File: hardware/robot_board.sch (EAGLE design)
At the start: 113 parts, among them J1 POWER_JACKPTH, U2 FT232RLSSOP

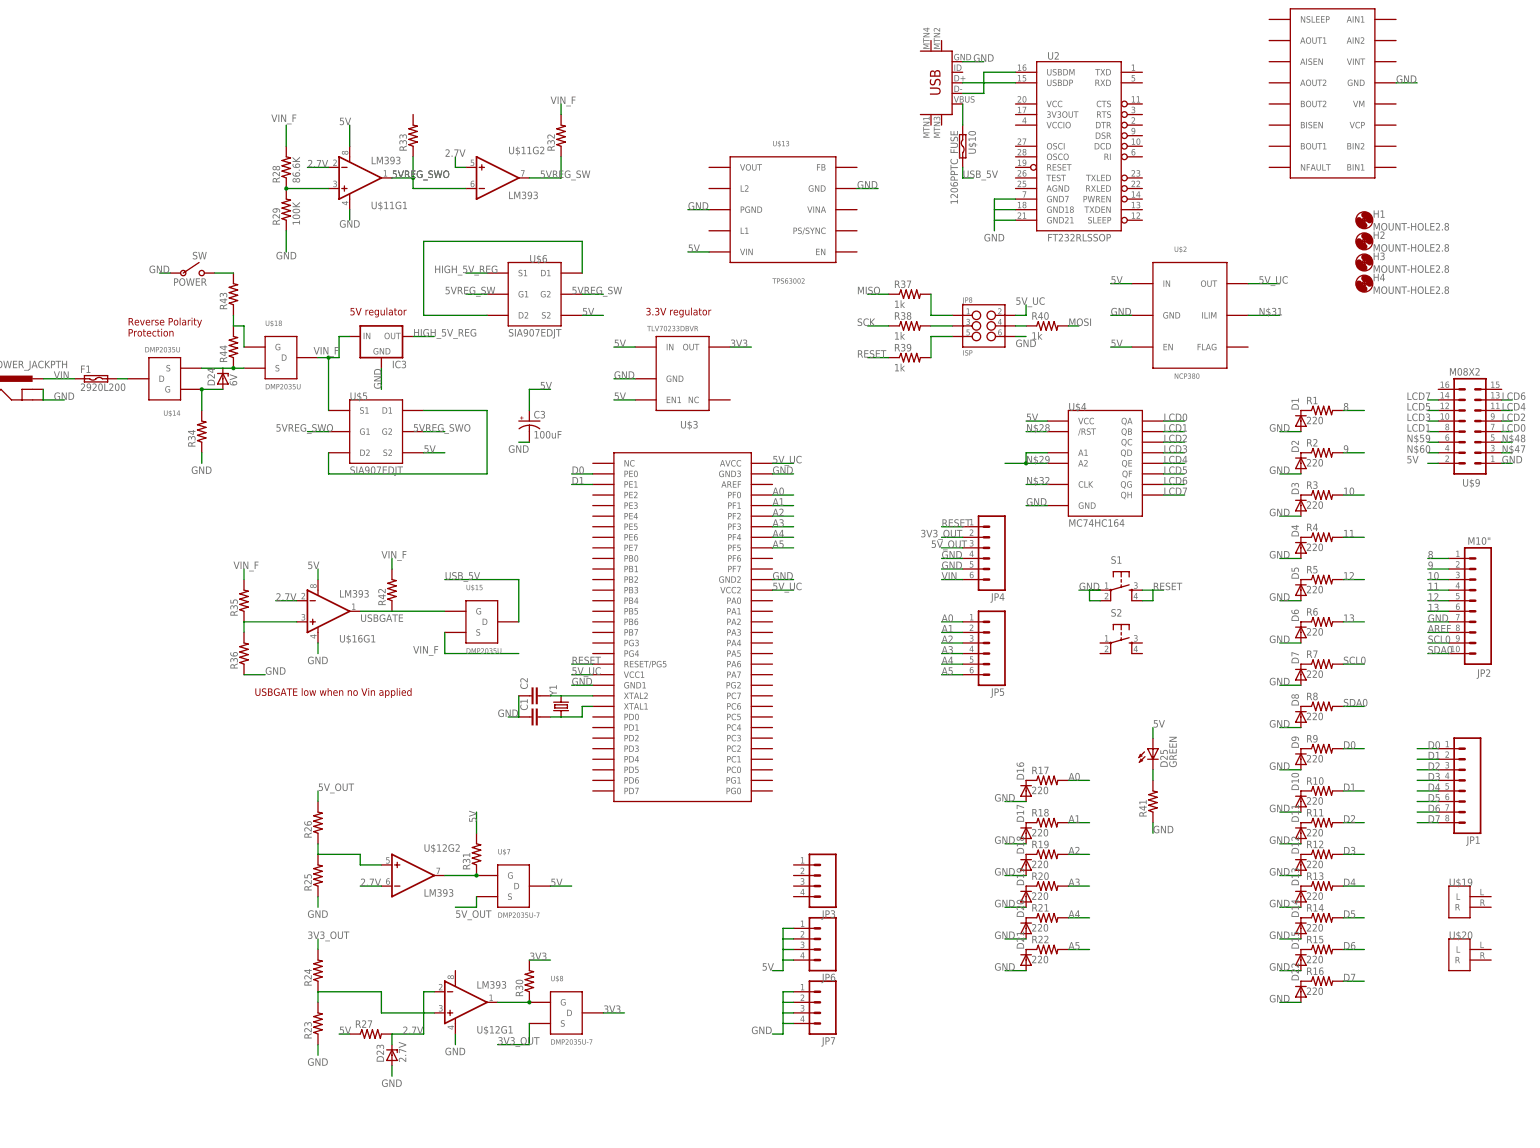
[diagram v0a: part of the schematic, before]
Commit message: check in library and restructured directories
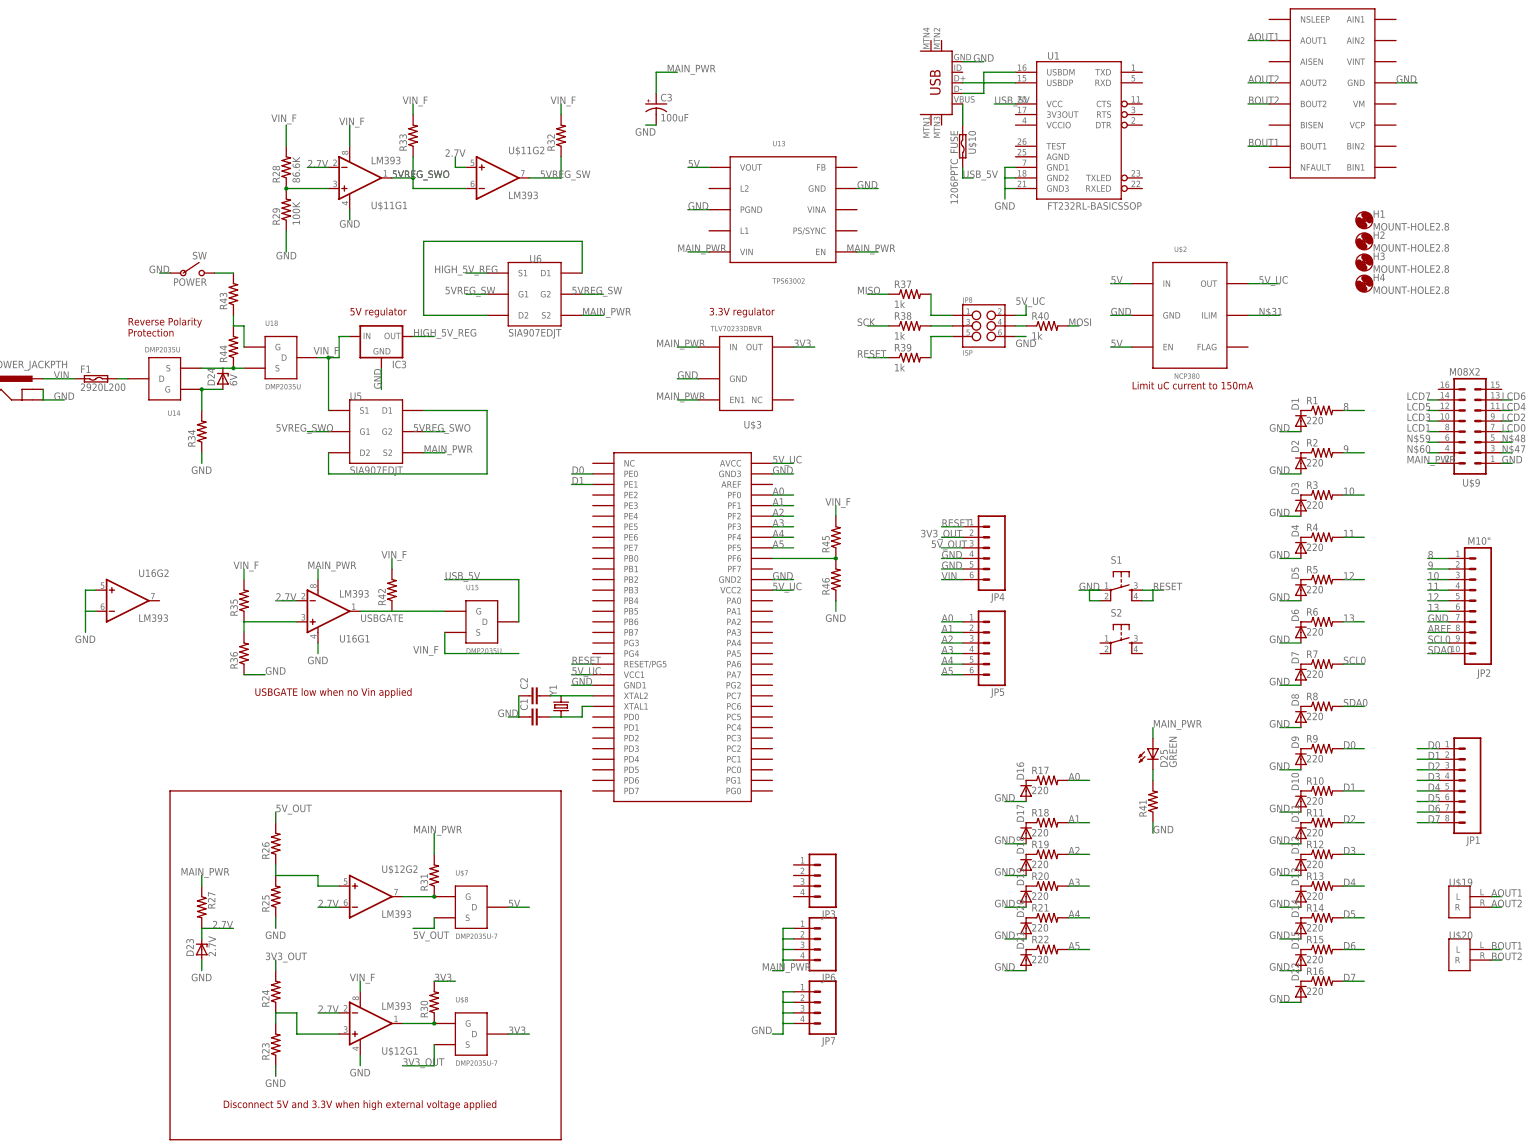
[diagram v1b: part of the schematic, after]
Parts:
- removed U$4: MC74HC164, r_cubed:MC74HC164
- removed U2: FT232RLSSOP, SparkFun-DigitalIC:FT232RLSSOP
- added R45, R46: (no value), resistor:R-US_R1206
- added U1: FT232RL-BASICSSOP, SparkFun-DigitalIC:FT232RL-BASICSSOP
- renumbered U$13 to U13, U$14 to U14, U$15 to U15, U$16 to U16, U$17 to U17, U$18 to U18, U$5 to U5, U$6 to U6
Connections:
- removed net N$28: U$4./RST
- removed net N$29: U$4.A1, U$4.A2
- removed net N$32: U$4.CLK
- new net AOUT1: U$19.L, U$21.AOUT1
- new net AOUT2: U$19.R, U$21.AOUT2
- new net BOUT1: U$20.L, U$21.BOUT1
- new net BOUT2: U$20.R, U$21.BOUT2
- new net MAIN_PWR: C3.+, D25.A, JP6.1, JP6.2, JP6.3, JP6.4, R27.1, R31.2, U$3.EN1, U$3.IN, U$9.2, U13.EN, U13.VIN, U16G1.V+, U5.S2, U6.S2
- new net N$52: R45.1, R46.2, U17.PF6
- net 5V: now also U13.VOUT; no longer C3.+, D25.A, JP6.1, JP6.2, JP6.3, JP6.4, R27.1, R31.2, U$11G1.V+, U$3.EN1, U$3.IN, U$4.VCC, U$9.2, U13.VIN, U16G1.V+, U5.S2, U6.S2
- net GND: now also R46.1, U16G2.+IN, U16G2.-IN; no longer U$4.GND, U2.GND18, U2.GND21, U2.GND7
- net LCD0: no longer U$4.QA
- net LCD1: no longer U$4.QB
- net LCD2: no longer U$4.QC
- net LCD3: no longer U$4.QD
- net LCD4: no longer U$4.QE
- net LCD5: no longer U$4.QF
- net LCD6: no longer U$4.QG
- net LCD7: no longer U$4.QH
- net N$1: now also U1.USBDM; no longer U2.USBDM
- net N$2: now also U1.USBDP; no longer U2.USBDP
- net USB_5V: now also U1.VCC
- net VIN_F: now also R33.2, R45.2, U$11G1.V+, U$12G1.V+
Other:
- note added: "Disconnect 5V and 3.3V when high external voltage applied"
- note added: "Limit uC current to 150mA"
- moved on the sheet: C3, D23, R23, R24, R25, R26, R27, R30, R31, U$12G1, U$12G2, U$3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

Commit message: updated schematic
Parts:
- removed U15: DMP2035U, jseng:DMP2035U
- added D26, D27, D28, D29: (no value), SparkFun-DiscreteSemi:DIODESOT23
- added R47, R48, R49, R50: 220, resistor:R-US_R1206
- added U2: NCP380, jseng:NCP380
- R30, R31, R32, R33, R34, R42: value (none) -> 10K
- U$2: value NCP380 -> SIA907EDJT; device jseng:NCP380 -> jseng:SIA907EDJT
- renumbered U$10 to F2, U$12 to U12, U$3 to U3, U$7 to U7, U$8 to U8
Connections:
- new net N$28: U$2.D1, U$2.D2
- new net N$29: D26.C, R47.1
- new net N$32: D27.C, R48.1
- new net N$53: D28.C, R49.1
- new net N$54: D29.C, R50.1
- new net SERVO0: JP3.1, R47.2
- new net SERVO1: JP3.2, R48.2
- new net SERVO2: JP3.3, R49.2
- new net SERVO3: JP3.4, R50.2
- net 5V: now also U13.FB, U2.EN, U2.IN; no longer U$2.EN, U$2.IN
- net 5V_UC: now also U2.OUT; no longer U$2.OUT
- net GND: now also D26.A, D27.A, D28.A, D29.A, U1.AGND, U1.GND1, U1.GND2, U1.GND3, U2.GND; no longer U$2.GND
- net MAIN_PWR: now also U13.PS/SYNC, U13.VINA
- net N$31: now also U2.ILIM; no longer U$2.ILIM
- net USBGATE: now also U$2.G1, U$2.G2; no longer U15.G
- net USB_5V: now also U$2.S1; no longer U15.D
- net VIN_F: now also U$2.S2; no longer U15.S
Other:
- note added: "Step-down 5V regulator"
- note added: "Step-up 5V regulator"
- note removed: "5V regulator"
- moved on the sheet: U$2

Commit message: update libraries
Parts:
- removed U$21: DRV8833, jseng:DRV8833
- added U$3: NRSINDUCTOR, jseng:NRSINDUCTOR
- added U$4, U$5: DRV8839, jseng:DRV8839
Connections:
- new net N$55: U$3.2, U13.L2
- new net N$56: U$3.1, U13.L1
- new net N$58: U$4.VM1, U$4.VM2
- new net N$61: U$5.VM1, U$5.VM2
- net 5V: now also U$4.NSLEEP, U$4.VCC, U$5.NSLEEP, U$5.VCC
- net AOUT1: now also U$4.OUT1; no longer U$21.AOUT1
- net AOUT2: now also U$4.OUT2; no longer U$21.AOUT2
- net BOUT1: now also U$5.OUT1; no longer U$21.BOUT1
- net BOUT2: now also U$5.OUT2; no longer U$21.BOUT2
- net GND: now also U$4.GND1, U$4.GND2, U$5.GND1, U$5.GND2; no longer U$21.GND
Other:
- moved on the sheet: D16, D17, D18, D19, D20, D21, D25, JP4, JP5, R17, R18, R19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

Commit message: added accelerometer device
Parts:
- removed U2: NCP380, jseng:NCP380
- removed U3: TLV70233DBVR, jseng:TLV70233DBVR
- added D30: GREEN, SparkFun-LED:LED-GREENLILYPAD
- added D31: YELLOW, SparkFun-LED:LED-GREENLILYPAD
- added R51, R52: 330, resistor:R-US_R1206
- added R53: 1.5K, resistor:R-US_R1206
- added R54: 10K, resistor:R-US_R1206
- added R55: 1K, resistor:R-US_R1206
- added U$6: MIC2009A, jseng:MIC2009A
- added U$7: TLV70233, jseng:TLV70233
- D23: value 2.7V -> 2.1V
- D25: value GREEN -> POWER
- R41: value (none) -> 330
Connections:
- net 10 renamed D10
- net 11 renamed D11
- net 12 renamed D12
- net 13 renamed D13
- net 2.7V renamed 2.1V
- net 8 renamed D8
- net 9 renamed D9
- net N$20 renamed D7_IN
- net N$29 renamed SERVO0_IN
- net N$32 renamed SERVO1_IN
- net N$5 renamed D8_IN
- net N$53 renamed SERVO2_IN
- net N$54 renamed SERVO3_IN
- net N$6 renamed D9_IN
- removed net N$10: D6.C, R6.1
- removed net N$11: D7.C, R7.1
- removed net N$12: D8.C, R8.1
- removed net N$13: D9.C, R9.1
- removed net N$14: D10.C, R10.1
- removed net N$15: D11.C, R11.1
- removed net N$16: D12.C, R12.1
- removed net N$17: D13.C, R13.1
- removed net N$18: D14.C, R14.1
- removed net N$19: D15.C, R15.1
- removed net N$21: D16.C, R17.1
- removed net N$22: D17.C, R18.1
- removed net N$23: D18.C, R19.1
- removed net N$24: D19.C, R20.1
- removed net N$25: D20.C, R21.1
- removed net N$26: D21.C, R22.1
- removed net N$31: U2.ILIM
- removed net N$58: U$4.VM1, U$4.VM2
- removed net N$61: U$5.VM1, U$5.VM2
- removed net N$7: D3.C, R3.1
- removed net N$8: D4.C, R4.1
- removed net N$9: D5.C, R5.1
- new net A0_IN: D16.C, R17.1, U17.PF0(ADC0)
- new net A1_IN: D17.C, R18.1, U17.PF1(ADC1)
- new net A2_IN: D18.C, R19.1, U17.PF2(ADC2)
- new net A3_IN: D19.C, R20.1, U17.PF3(ADC3)
- new net A4_IN: D20.C, R21.1, U17.PF4(ADC4)
- new net A5_IN: D21.C, R22.1, U17.PF5(ADC5)
- new net D0_IN: D9.C, R9.1, U17.PE0(TXD)
- new net D1_IN: D10.C, R10.1, U17.PE1(RXD)
- new net D2_IN: D11.C, R11.1, U17.PE2
- new net D3_IN: D12.C, R12.1, U17.PE3
- new net D4_IN: D13.C, R13.1, U17.PE6
- new net D5_IN: D14.C, R14.1, U17.PB5(OC1A)
- new net D6_IN: D15.C, R15.1, U17.PB6(OC1B)
- new net LED0: D30.A, U17.PG0
- new net LED1: D31.A, U17.PG1
- new net M0_DIR0: U$4.IN1, U17.PD4
- new net M0_DIR1: U$4.IN2, U17.PD5
- new net M0_EN: U$4.EN1, U$4.EN2, U17.PB4(OC0A)
- new net M1_DIR0: U$5.IN1, U17.PD6
- new net M1_DIR1: U$5.IN2, U17.PD7
- new net M1_EN: U$5.EN1, U$5.EN2, U17.PB7(OC2A)
- new net N$5: R53.2, U$6.ILIM
- new net N$57: D30.C, R51.2
- new net N$6: R55.2, U17.PG2
- new net N$62: D31.C, R52.2
- new net SCL_IN: D7.C, R7.1, U17.PE4(SCL)
- new net SDA_IN: D8.C, R8.1, U17.PE5(SDA)
- new net SS: D3.C, R3.1, U17.PB0(SS)
- net 3V3: now also U$7.OUT; no longer U3.OUT
- net 5V: now also U$6.VIN; no longer U2.EN, U2.IN
- net 5V_UC: no longer U2.OUT
- net A0: no longer U17.PF0
- net A1: no longer U17.PF1
- net A2: no longer U17.PF2
- net A3: no longer U17.PF3
- net A4: no longer U17.PF4
- net A5: no longer U17.PF5
- net AREF: now also U17.AREF
- net D0: no longer U17.PE0
- net D1: no longer U17.PE1
- net GND: now also R51.1, R52.1, R53.1, R54.1, U$7.GND; no longer U2.GND, U3.GND
- net MAIN_PWR: now also U$7.EN1, U$7.IN; no longer U3.EN1, U3.IN
- net MISO: now also D5.C, R5.1, U17.PB3(MISO)
- net MOSI: now also D4.C, R4.1, U17.PB2(MOSI)
- net N$52: now also U17.PF6(ADC6); no longer U17.PF6
- net SCK: now also D6.C, R6.1, U17.PB1(SCK)
- net USB_5V: now also R54.2, R55.1
- net VIN_F: now also U$4.VM1, U$4.VM2, U$5.VM1, U$5.VM2
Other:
- moved on the sheet: D16, D17, D19, D20, D21, D25, D27, D28, D29, R17, R18, R20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

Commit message: changed board size and added gyro interrupt
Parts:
- added C4: .1uF, resistor:C-USC1206
- added R56: 1K, resistor:R-US_R1206
- added U$8: MMA8453Q, jseng:MMA8453Q
- R23, R24, R25, R26, R27: device resistor:R-US_R0805 -> resistor:R-US_R1206
- R28: value 86.6K -> (none); device resistor:R-US_R0805 -> resistor:R-US_R1206
- R29: value 100K -> (none); device resistor:R-US_R0805 -> resistor:R-US_R1206
- R30, R31, R32, R33: value 10K -> (none); device resistor:R-US_R0805 -> resistor:R-US_R1206
- R37, R38: value 1k -> 4.7K
- R40: value 1k -> 10K
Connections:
- removed net N$37: JP8.4, R40.1
- removed net N$49: JP8.3, R38.2
- removed net N$50: JP8.1, R37.2
- new net DTR: C4.1, U1.DTR
- new net GYRO_INT: U$8.INT1, U17.PD1
- new net LCD_E: U17.PG4
- new net LCD_RS: U17.PG3
- new net N$7: JP4.1, R56.2
- new net SW1: S2.3, S2.4
- net 2.1V: now also R23.1; no longer R27.2
- net 3V3: now also R37.2, R38.2, U$8.NC4, U$8.NC5, U$8.VDD, U$8.VDDIO
- net 3V3_OUT: now also R27.2; no longer R24.2
- net 5VREG_SW: now also R33.1; no longer R32.1
- net 5VREG_SWO: now also R32.1; no longer R33.1
- net 5V_OUT: now also R24.2; no longer R26.2
- net 5V_UC: now also R40.1
- net D0_IN: now also U17.PE0(RXD); no longer U17.PE0(TXD)
- net D11: now also JP8.4
- net D12: now also JP8.1
- net D13: now also JP8.3
- net D1_IN: now also U17.PE1(TXD); no longer U17.PE1(RXD)
- net GND: now also R26.1, R28.1, R31.1, S2.1, S2.2, U$8.GND1, U$8.GND2, U$8.GND3, U$8.NC2, U$8.NC3, U$8.SA0; no longer R23.1, R25.1, R29.1
- net LCD0: now also U17.PA0
- net LCD1: now also U17.PA1
- net LCD2: now also U17.PA2
- net LCD3: now also U17.PA3
- net LCD4: now also U17.PA4
- net LCD5: now also U17.PA5
- net LCD6: now also U17.PA6
- net LCD7: now also U17.PA7
- net MAIN_PWR: now also R23.2, R25.2; no longer R27.1, R31.2
- net MISO: no longer R37.1
- net MOSI: no longer R40.2
- net N$3: now also U17.XTAL2
- net N$30: now also R25.1; no longer R31.1
- net N$34: now also R24.1, R26.2; no longer R25.2, R26.1
- net N$35: now also R28.2, R29.1; no longer R28.1, R29.2
- net N$38: now also R27.1, R31.2; no longer R23.2, R24.1
- net N$4: now also U17.XTAL1
- net RESET: now also C4.2, R40.2, R56.1; no longer JP4.1
- net SCK: no longer R38.1
- net SCL_IN: now also R38.1, U$8.SCL
- net SDA_IN: now also R37.1, U$8.SDA
- net VIN_F: now also R29.2; no longer R28.2
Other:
- moved on the sheet: C1, C2, D16, D17, D18, D19, D20, D21, D25, D30, D31, JP4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

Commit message: modified overall layout
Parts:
- removed D24: 6V, diode:ZENER-DIODESOD80C
- removed U$1: USB-MINIB-5PIN, SparkFun-Connectors:USB-MINIB-5PIN
- removed U$3: NRSINDUCTOR, jseng:NRSINDUCTOR
- removed U13: TPS63002, jseng:TPS63002
- added C5: .1uF, resistor:C-USC1206
- added JP9: USB-B, SparkFun-Connectors:USBPTH
- renumbered U$11 to U11, U14 to Q1, U18 to Q2, U7 to Q3, U8 to Q4
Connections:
- removed net N$27: F2.1, U$1.VBUS
- removed net N$55: U$3.2, U13.L2
- removed net N$56: U$3.1, U13.L1
- new net N$31: U$6.FAULT
- new net N$8: C5.1, U$8.BYP
- new net N$9: F2.1, JP9.VBUS
- net 5V: now also U$6.EN; no longer U13.FB, U13.VOUT
- net 5V_UC: now also U$6.VOUT
- net GND: now also C5.2, JP9.GND, U$6.GND; no longer U$1.GND, U13.GND, U13.PGND
- net MAIN_PWR: no longer U13.EN, U13.PS/SYNC, U13.VIN, U13.VINA
- net N$1: now also JP9.D-; no longer U$1.D-
- net N$2: now also JP9.D+; no longer U$1.D+
- net N$36: no longer D24.A
- net N$40: no longer D24.C
- net USB_5V: now also U1.VCCIO
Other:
- note removed: "Step-up 5V regulator"
- moved on the sheet: F2, R37, R38

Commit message: begin power layout
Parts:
- removed IC3: (no value), v-reg:78XXS
- added U3: MIC5219, SparkFun-PowerIC:MIC52055V
- C1, C2: value (none) -> 22pF
- R1, R10, R11, R12, R13, R14, R15, R16, R17, R18, R19, R2, R20, R21, R22, R3, R4, R47, R48, R49, R5, R50, R6, R7, R8, R9: value 220 -> 300
- R25, R30, R32, R33: value (none) -> 10K
- R43: value (none) -> 1K
- R44: value (none) -> 100K
- Y1: value (none) -> 16MHz
- renumbered U$2 to U2, U$7 to U7
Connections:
- net GYRO_INT renamed ACCEL_INT
- removed net MAIN_PWR: C3.+, D25.A, JP6.1, JP6.2, JP6.3, JP6.4, R23.2, R25.2, U$9.2, U16G1.V+, U5.S2, U6.S2, U7.EN1, U7.IN
- removed net N$40: Q1.S, Q2.S, R44.1
- new net PWR_SW: Q1.S, Q2.S, R44.1, U2.S2
- new net RX: U1.TXD, U17.PD3
- new net TX: U1.RXD, U17.PD2
- net 5V: now also C3.+, D25.A, JP6.1, JP6.2, JP6.3, JP6.4, R23.2, R25.2, U$9.2, U5.S2, U6.S2, U7.EN1, U7.IN
- net GND: now also U3.GND; no longer IC3.GND
- net HIGH_5V_REG: now also U3.OUT; no longer IC3.OUT
- net USB_5V: now also U16G1.V+
- net VIN: now also R35.2
- net VIN_F: now also U3.EN, U3.IN; no longer IC3.IN, R35.2, U2.S2
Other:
- moved on the sheet: U6

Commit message: more routing and library updates
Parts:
- added IR: (no value), SparkFun-Connectors:M03PTH
- added JP10, JP11: (no value), SparkFun-Connectors:M03X22X3_SILK_SM
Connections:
- net N$33: now also JP4.6
- net VIN: no longer JP4.6
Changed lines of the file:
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@@
 <part name="JP9" library="SparkFun-Connectors" deviceset="USB" device="PTH" value="USB-B"/>
 <part name="U3" library="SparkFun-PowerIC" deviceset="MIC5205" device="5V" value="MIC5219"/>
+<part name="JP10" library="SparkFun-Connectors" deviceset="M03X2" device="2X3_SILK_SM"/>
+<part name="JP11" library="SparkFun-Connectors" deviceset="M03X2" device="2X3_SILK_SM"/>
+<part name="IR" library="SparkFun-Connectors" deviceset="M03" device="PTH"/>
 </parts>
 <sheets>
@@
 <instance part="JP9" gate="G$1" x="170.18" y="172.72" rot="R180"/>
 <instance part="U3" gate="G$1" x="50.8" y="101.6"/>
+<instance part="JP10" gate="G$1" x="-27.94" y="167.64"/>
+<instance part="JP11" gate="G$1" x="-25.4" y="152.4"/>
+<instance part="IR" gate="G$1" x="342.9" y="81.28" rot="R180"/>
 </instances>
 <busses>
@@
 <net name="VIN" class="0">
 <segment>
-<pinref part="JP4" gate="G$1" pin="6"/>
-<wire x1="226.06" y1="-55.88" x2="220.98" y2="-55.88" width="0.1524" layer="91"/>
-<label x="220.98" y="-55.88" size="1.778" layer="95"/>
-</segment>
-<segment>
 <pinref part="J1" gate="G$1" pin="PWR"/>
 <wire x1="-40.64" y1="93.98" x2="-33.02" y2="93.98" width="0.1524" layer="91"/>
@@
 <wire x1="-22.86" y1="93.98" x2="-20.32" y2="93.98" width="0.1524" layer="91"/>
 <pinref part="Q1" gate="G$1" pin="D"/>
-</segment>
-</net>
+<label x="-22.86" y="93.98" size="1.778" layer="95"/>
+</segment>
+<segment>
+<pinref part="JP4" gate="G$1" pin="6"/>
+<wire x1="226.06" y1="-55.88" x2="220.98" y2="-55.88" width="0.1524" layer="91"/>
+<label x="220.98" y="-55.88" size="1.778" layer="95"/>
+</segment>
+</net>
